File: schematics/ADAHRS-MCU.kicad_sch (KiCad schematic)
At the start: 40 parts, among them J1 Conn_02x05_Odd_Even, Y1 16 MHz crystal osc

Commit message: v1.05
I wanted to save all the global labels and progress. I noticed my program glitching and would like to double check this file incase of any parts that might get messed up.
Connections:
- net MCU GPIO/DRDY: no longer U-TMS570LS20216-EP1.134 (GIOA[1]/INT1)
- net MCU GPIO/rSTART: no longer U-TMS570LS20216-EP1.118 (GIOA[0]/INT0)
- net MCU SPI MISO/DOUT: now also U-TMS570LS20216-EP1.5 (MIBSPI3SOMI); no longer U-TMS570LS20216-EP1.13 (MIBSPI1SOMI)
- net MCU SPI MOSI/rDIN: now also U-TMS570LS20216-EP1.4 (MIBSPI3SIMO); no longer U-TMS570LS20216-EP1.14 (MIBSPI1SIMO)
- net MCU SPI SCLK: now also U-TMS570LS20216-EP1.3 (MIBSPI3CLK); no longer U-TMS570LS20216-EP1.17 (MIBSPI1CLK)
- net MCU NHET0/EN: now reaches U-TMS570LS20216-EP1.105 (NHET[0])
- net MCU gyro y CS: now reaches U-TMS570LS20216-EP1.24 (MIBSPI1CS[1])
- net MCU gyro z CS: now reaches U-TMS570LS20216-EP1.25 (MIBSPI1CS[2])
- net MCU NHET3/EN: now reaches U-TMS570LS20216-EP1.41 (NHET[3])
- net MCU NHET1/EN: now reaches U-TMS570LS20216-EP1.42 (NHET[1])
- net MCU NHET2/EN: now reaches U-TMS570LS20216-EP1.56 (NHET[2])
- net MCU all analog SPI/CS: now reaches U-TMS570LS20216-EP1.7 (MIBSPI3CS[0])
- net MCU SCLK ADXL: now reaches U-TMS570LS20216-EP1.91 (MIBSPI5CLK/DMMDATA[4])
- net MCU CS ADXL: now reaches U-TMS570LS20216-EP1.92 (MIBSPI5CS[0]/DMMDATA[5])
- net MCU MOSI ADXL: now reaches U-TMS570LS20216-EP1.95 (MIBSPI5SIMO[0]/DMMDATA[8])
- net MCU MISO ADXL: now reaches U-TMS570LS20216-EP1.99 (MIBSPI5SOMI[0]/DMMDATA[12])
- net GPIO #2 renamed MCU GPIO 2 DRDY
- net GPIO #3: no longer names the net of U-TMS570LS20216-EP1.144 (GIOA[3]/INT3)
- net MCU SPI/CS renamed MCU gyro x CS
- new net MCU GPIO 0 INT2: U-TMS570LS20216-EP1.118 (GIOA[0]/INT0)
- new net MCU GPIO 1 INT1: U-TMS570LS20216-EP1.134 (GIOA[1]/INT1)
- new net MCU MISO GYRO X : U-TMS570LS20216-EP1.13 (MIBSPI1SOMI)
- new net MCU MOSI GYRO X : U-TMS570LS20216-EP1.14 (MIBSPI1SIMO)
- new net MCU SCLK GYRO X: U-TMS570LS20216-EP1.17 (MIBSPI1CLK)
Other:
- note added: "barometer"
- note added: "magnetometer"
- note added: "outside temp"

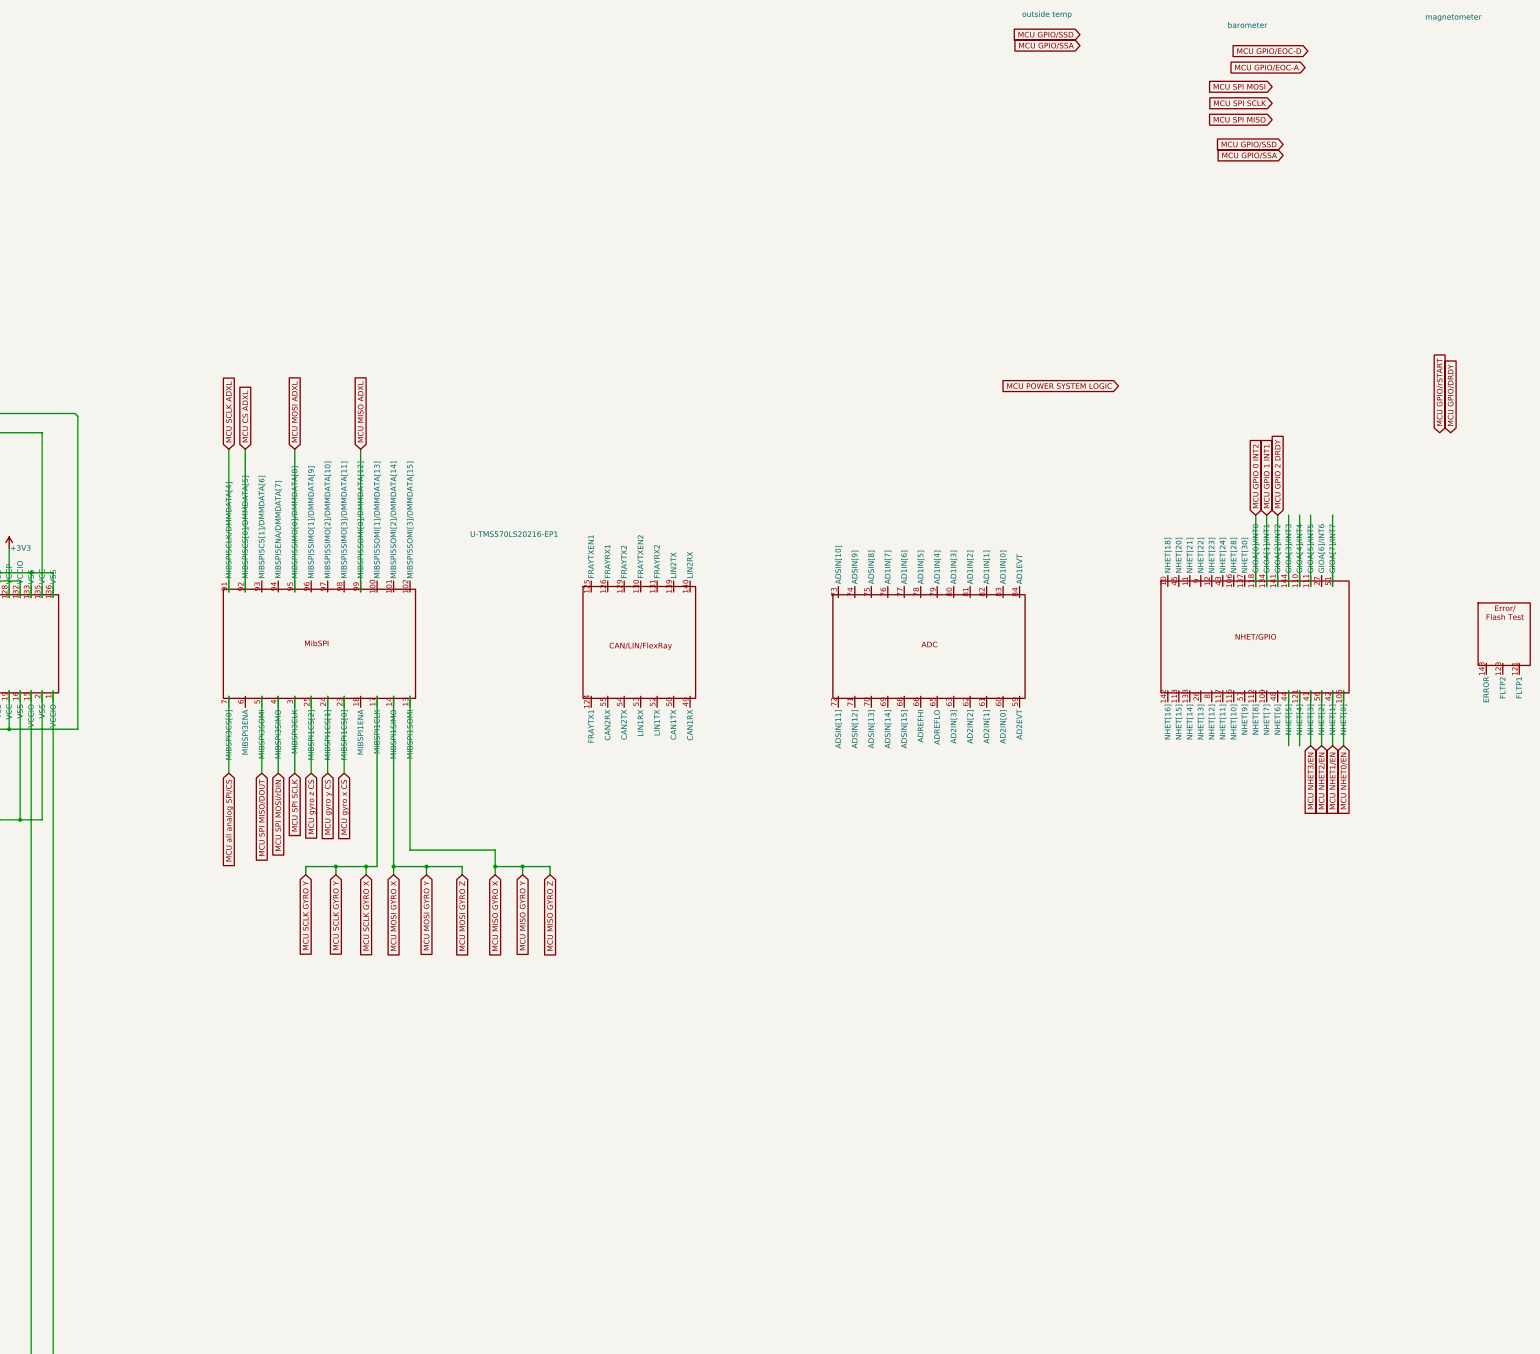
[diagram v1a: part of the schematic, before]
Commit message: v1.06
I still need to double check the wiring. Additionally, I did not read much about the error/flash test yet. I did create the custom HI-35870 symbol and wired the power. I need to check for caps and passive components.
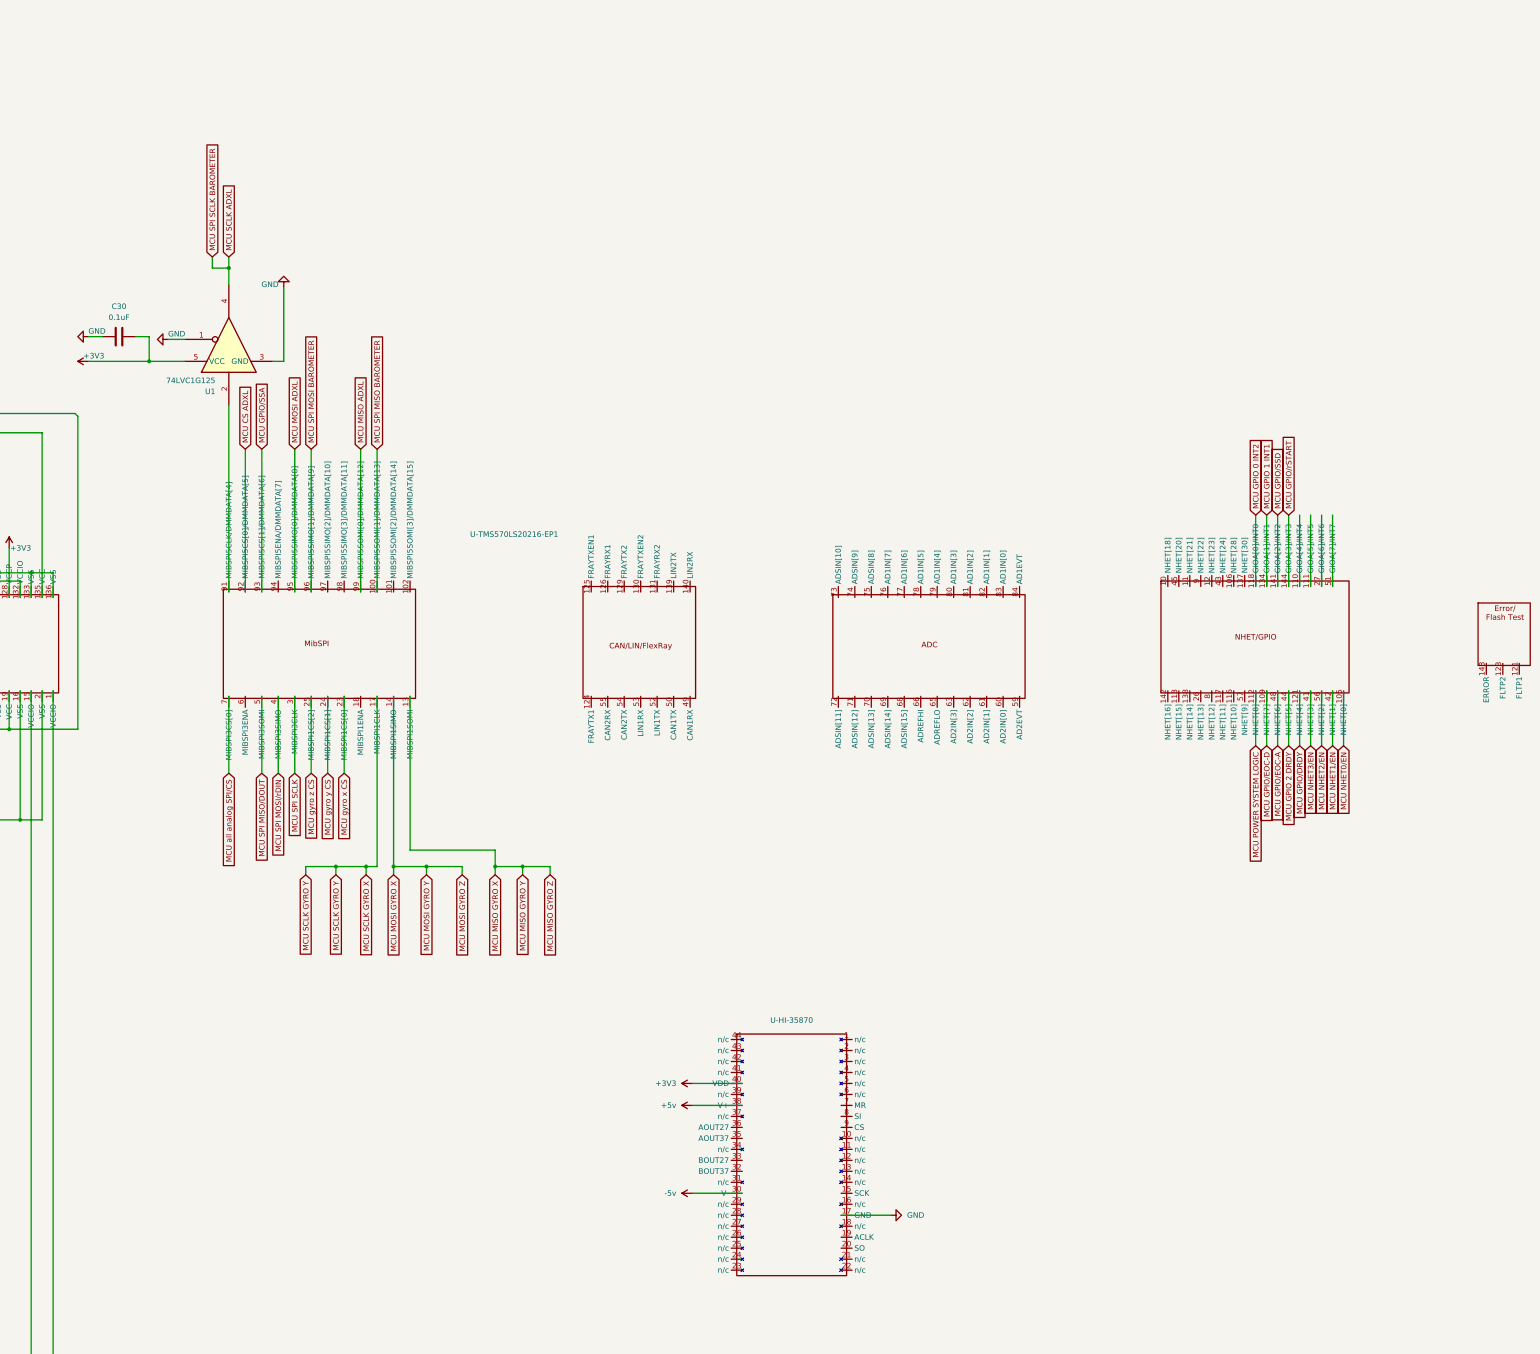
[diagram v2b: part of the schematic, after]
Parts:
- added C30: 0.1uF, symbol Device:C
- added U-HI-35870: ~, symbol custom:HI-35870
- added U1: 74LVC1G125, symbol 74xGxx:74LVC1G125
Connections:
- net +3V3: now also C30.2, U-HI-35870.40 (VDD), U1.5 (VCC)
- net GND: now also C30.1, U-HI-35870.17 (GND), U1.1, U1.3 (GND)
- net MCU GPIO 2 DRDY: now also U-TMS570LS20216-EP1.44 (NHET[5]); no longer U-TMS570LS20216-EP1.141 (GIOA[2]/INT2)
- net MCU GPIO/DRDY: now also U-TMS570LS20216-EP1.121 (FLTP1)
- net MCU GPIO/EOC-A: now also U-TMS570LS20216-EP1.48 (NHET[6])
- net MCU GPIO/EOC-D: now also U-TMS570LS20216-EP1.109 (NHET[7])
- net MCU GPIO/SSA: now also U-TMS570LS20216-EP1.93 (MIBSPI5CS[1]/DMMDATA[6])
- net MCU GPIO/SSD: now also U-TMS570LS20216-EP1.141 (GIOA[2]/INT2)
- net MCU GPIO/rSTART: now also U-TMS570LS20216-EP1.144 (GIOA[3]/INT3)
- net MCU POWER SYSTEM LOGIC: now also U-TMS570LS20216-EP1.112 (NHET[8])
- net MCU SCLK ADXL: now also U1.4; no longer U-TMS570LS20216-EP1.91 (MIBSPI5CLK/DMMDATA[4])
- net MCU SPI MISO BAROMETER: now reaches U-TMS570LS20216-EP1.100 (MIBSPI5SOMI[1]/DMMDATA[13])
- net MCU SPI MOSI BAROMETER: now reaches U-TMS570LS20216-EP1.96 (MIBSPI5SIMO[1]/DMMDATA[9])
- new net: U-TMS570LS20216-EP1.91 (MIBSPI5CLK/DMMDATA[4]), U1.2
- new net +5v: U-HI-35870.38 (V+)
- new net -5v: U-HI-35870.30 (V-)
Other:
- note removed: "barometer"
- note removed: "magnetometer"
- note removed: "outside temp"

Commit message: mcu v1.07
I added test pins, switched regulator, finished the transmitter for arinc 429 connection, and renamed global labels.
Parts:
- removed U1: 74LVC1G125, symbol 74xGxx:74LVC1G125
- added C29, C31, C32: 0.1uF, symbol Device:C
- added J3: Connector_Molex:Molex_Micro-Fit_3.0_43045-0200_2x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, Connector_Molex:Molex_Micro-Fit_3.0_43045-0200_2x01_P3.00mm_Horizontal, symbol Connector_Generic:Conn_01x02
- added R10: 10k, symbol Device:R
- added SN74LVC3G1, SN74LVC3G34: 74LVC3G34, symbol 74xGxx:74LVC3G34
- added TP1, TP2: TestPoint, symbol Connector:TestPoint
- added U1: LM2776, Package_TO_SOT_SMD:SOT-23-6, symbol Regulator_SwitchedCapacitor:LM2776
- C30: value 0.1uF -> 1uF
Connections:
- net +3.3V is gone; now on net +3V3: J1.1 (Pin_1)
- net MCU GPIO 2 DRDY is gone; now on net MCU GPIO/EOC-A: U-TMS570LS20216-EP1.44 (NHET[5])
- net MCU NHET3/EN is gone; now on net MCU GPIO/DRDY: U-TMS570LS20216-EP1.41 (NHET[3])
- net MCU SPI SCLK is gone; now on an unnamed net: U-TMS570LS20216-EP1.3 (MIBSPI3CLK)
- net +3V3: now also U-TMS570LS20216-EP1.66 (ADREFHI); no longer C30.2
- net +5v: now also C29.1, U1.3 (VIN); no longer U-HI-35870.38 (V+)
- net GND: now also U-TMS570LS20216-EP1.65 (ADREFLO), C29.2, C31.1, C32.1, R10.1; no longer C30.1
- net MCU GPIO/DRDY: no longer U-TMS570LS20216-EP1.121 (FLTP1)
- net MCU GPIO/EOC-A: no longer U-TMS570LS20216-EP1.48 (NHET[6])
- net MCU GPIO/EOC-D: now also U-TMS570LS20216-EP1.48 (NHET[6]); no longer U-TMS570LS20216-EP1.109 (NHET[7])
- net MCU POWER SYSTEM LOGIC: now also U-TMS570LS20216-EP1.109 (NHET[7]); no longer U-TMS570LS20216-EP1.112 (NHET[8])
- net MCU SCLK ADXL: now also SN74LVC3G34.7
- net MCU SCLK GYRO X: now also SN74LVC3G1.7; no longer U-TMS570LS20216-EP1.17 (MIBSPI1CLK)
- net at U-HI-35870.19 (ACLK): now also U-TMS570LS20216-EP1.112 (NHET[8])
- net at U-HI-35870.20 (SO): now also U-TMS570LS20216-EP1.101 (MIBSPI5SOMI[2]/DMMDATA[14])
- net at U-HI-35870.32 (BOUT37): now also J3.1 (Pin_1)
- net at U-HI-35870.35 (AOUT37): now also J3.2 (Pin_2)
- net at U-HI-35870.7 (MR): now also U-TMS570LS20216-EP1.116 (NHET[10])
- net at U-HI-35870.8 (SI): now also U-TMS570LS20216-EP1.97 (MIBSPI5SIMO[2]/DMMDATA[10])
- net at U-HI-35870.9 (CS): now also U-TMS570LS20216-EP1.57 (NHET[9])
- net at U-TMS570LS20216-EP1.117 (NHET[11]): now also R10.2, U1.4 (EN)
- net MCU GPIO DRDY accel: now reaches U-TMS570LS20216-EP1.121 (FLTP1)
- net at U-TMS570LS20216-EP1.123 (FLTP2): now also TP1.1
- net MCU POWER SYSTEM LOGIC ERROR: now reaches U-TMS570LS20216-EP1.143 (ERROR)
- net at U-TMS570LS20216-EP1.91 (MIBSPI5CLK/DMMDATA[4]): now also SN74LVC3G34.1
- new net: SN74LVC3G1.1, U-TMS570LS20216-EP1.17 (MIBSPI1CLK)
- new net: C32.2, U-HI-35870.38 (V+), U1.1 (VOUT)
- new net: C31.2, U1.2 (GND)
- new net: C30.1, U1.5 (C1+)
- new net: C30.2, U1.6 (C1-)
- new net: TP2.1, U-TMS570LS20216-EP1.121 (FLTP1)
- no-connect marks 7 -> 45

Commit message: mcu power rails v1.08
I added the ref power rails to simplify designs and remove excess switch regulators. as I am finalizing the schematic captures, I will need to remove excess unless needed there.
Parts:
- added C34, C35, C37, C38: 10uF, symbol Device:C
- added L1, L2: L0.47uH, symbol Device:L
- added R11: 76.8kΩ, symbol Device:R
- added R12: 51kΩ, symbol Device:R
- added R8: 88.7kΩ, symbol Device:R
- added R9: 19.6kΩ, symbol Device:R
- added U-FMCE-0828: ~, symbol custom:FMCE-0828
- added U-MFL2805S1: ~, symbol custom:MFL2805S
- added U-TPS1: ~, symbol custom:TPS62442
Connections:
- net +5v: now also U-HI-35870.38 (V+), U-TPS1.10 (EN2), U-TPS1.11 (VIN2), U-TPS1.7 (VIN1), U-TPS1.8 (EN1)
- net -5v: now also C32.2, U1.1 (VOUT)
- net GND: now also C34.1, C35.1, C37.1, C38.1, R12.1, R9.1, U-TPS1.14 (COMP/FSET), U-TPS1.5 (MODE/SYNC), U-TPS1.9 (GND)
- new net: R11.1, R12.2, U-TPS1.1 (FB2)
- new net: U-FMCE-0828.2 (+VOUT), U-MFL2805S1.1 (POSITIVE_INPUT)
- new net: U-FMCE-0828.3 (OUT_COM), U-MFL2805S1.2 (INPUT_COMMON), U-MFL2805S1.6 (SYNC_IN)
- new net: L2.1, U-TPS1.12 (SW2)
- new net: R8.1, R9.2, U-TPS1.3 (FB1)
- new net: L1.2, U-TPS1.6 (SW1)
- new net +1V5 rail: C37.2, C38.2, L2.2, R11.2
- new net +28V: U-FMCE-0828.1 (+VIN)
- new net +3V3 rail: C34.2, C35.2, L1.1, R8.2
- new net +5V rail: U-MFL2805S1.10 (POSITIVE_SENSE), U-MFL2805S1.7 (POSITIVE_OUTPUT)
- new net CHASSIS: U-FMCE-0828.4 (CASE_GND)
- new net Power bus GND: U-FMCE-0828.5 (IN_COM)
- new net ref GND: U-MFL2805S1.8 (OUTPUT_COMMON), U-MFL2805S1.9 (SENSE_RETURN)
- no-connect marks 45 -> 50
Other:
- moved on the sheet: C16, C17, C18, C19, C20, C21, C22, J3, R3
